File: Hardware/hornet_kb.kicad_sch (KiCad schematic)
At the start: 28 parts, among them J1 Conn_ST_STDC14, J10 USB_C_Receptacle_USB2.0, SW98 SW_Push, U1 nRF52840, Y1 32.768kHz, Y2 32MHz

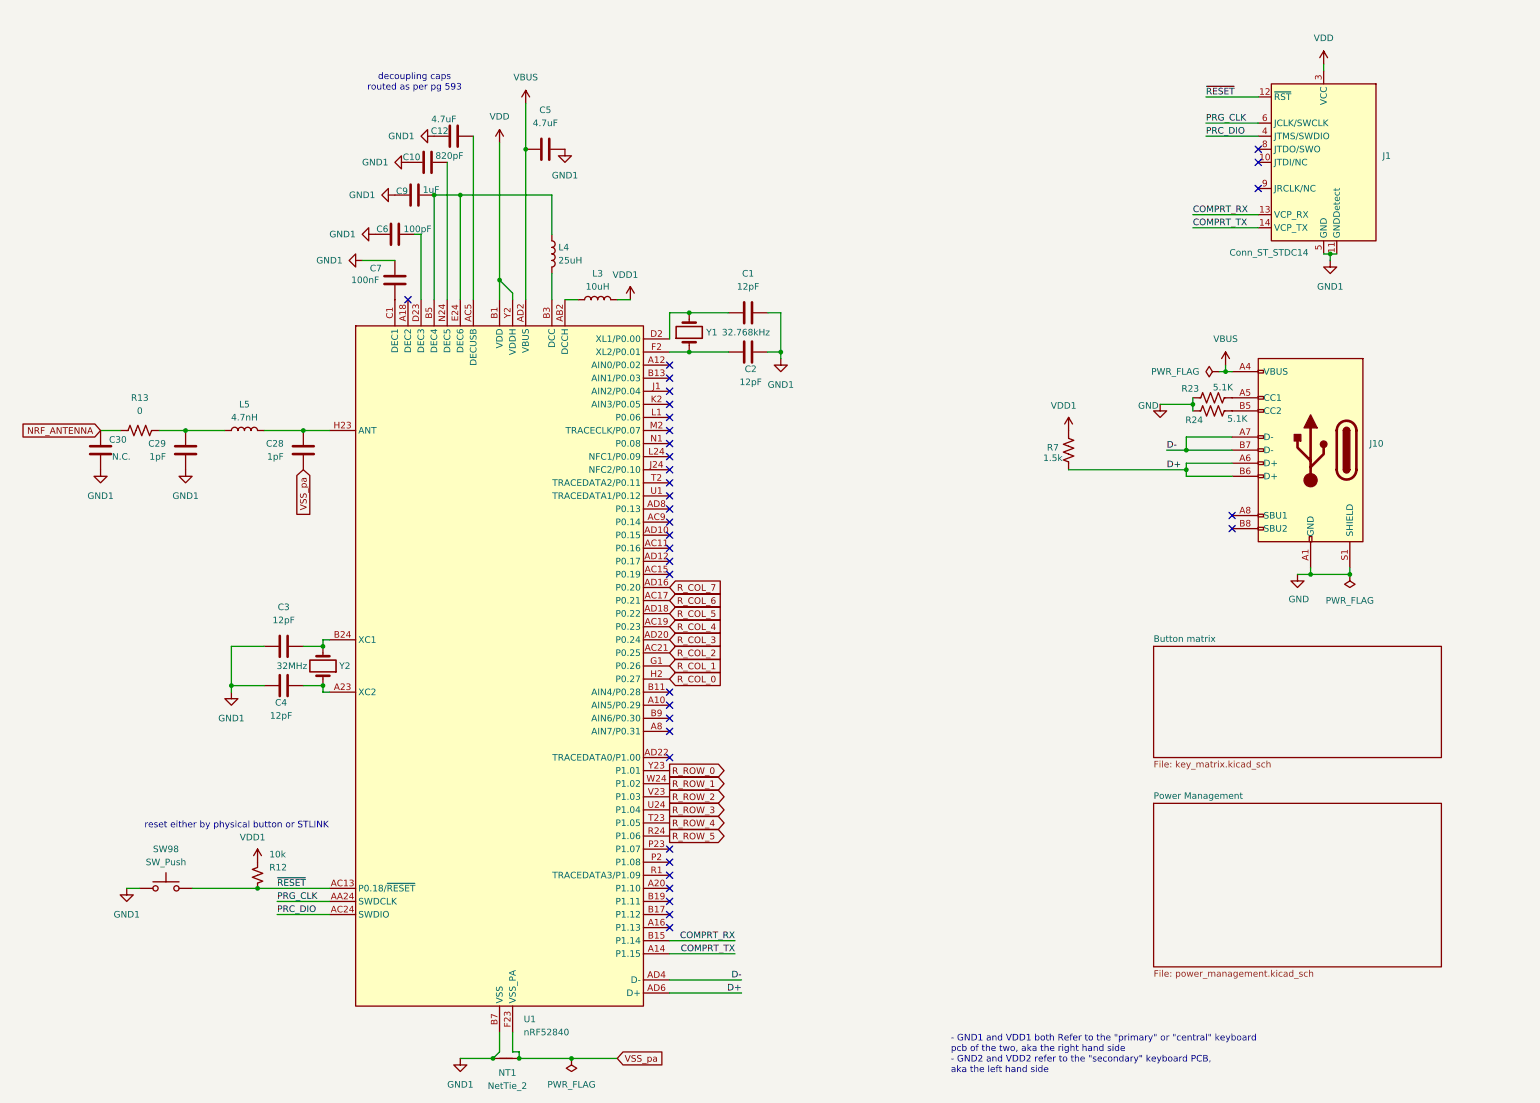
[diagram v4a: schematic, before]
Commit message: Change labels from global to netlist
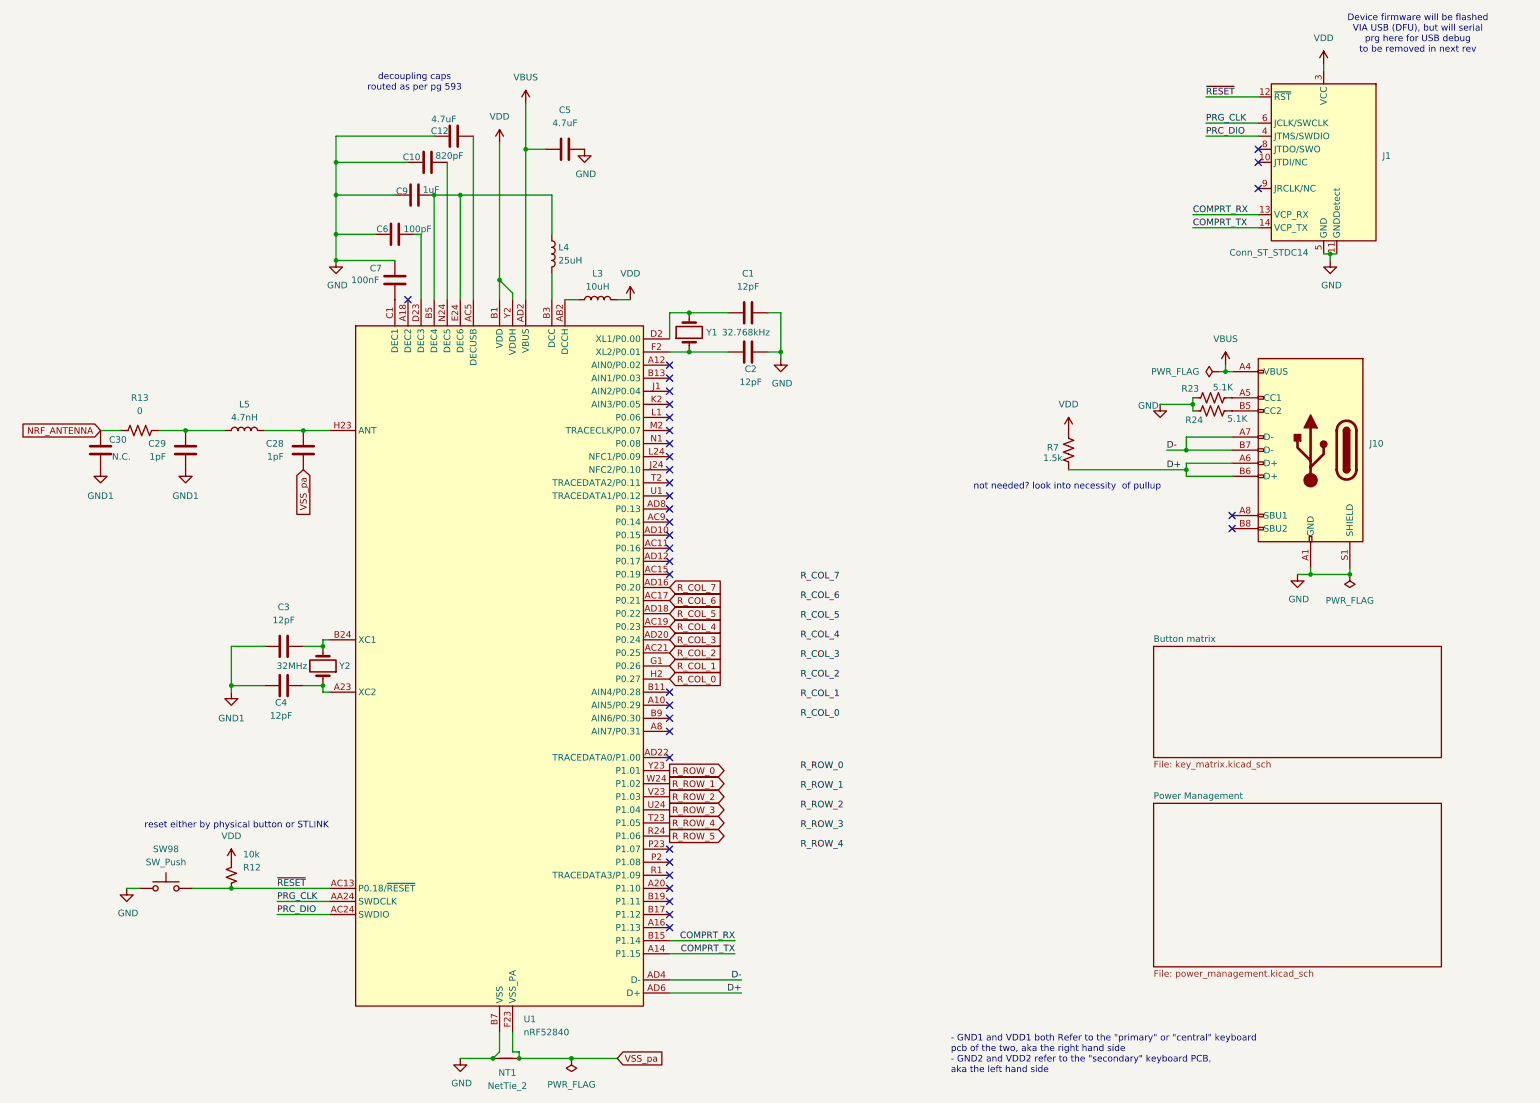
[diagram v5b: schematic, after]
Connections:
- net VDD1 is gone; now on net VDD: L3.1, R12.1, R7.1
- net GND: now also C1.1, C10.1, C12.2, C2.1, C5.1, C6.2, C7.2, C9.2, J1.11 (GNDDetect), J1.5 (GND), J1.7 (GND), NT1.2, SW98.2, U1.B7 (VSS), U1.EP (VSS)
- net GND1: no longer C1.1, C10.1, C12.2, C2.1, C5.1, C6.2, C7.2, C9.2, J1.11 (GNDDetect), J1.5 (GND), J1.7 (GND), NT1.2, SW98.2, U1.B7 (VSS), U1.EP (VSS)
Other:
- note added: "Device firmware will be flashed VIA USB (DFU), but will serial prg here for USB debug to be removed in next rev"
- note added: "not needed? look into necessity of pullup"
- moved on the sheet: C5, R12

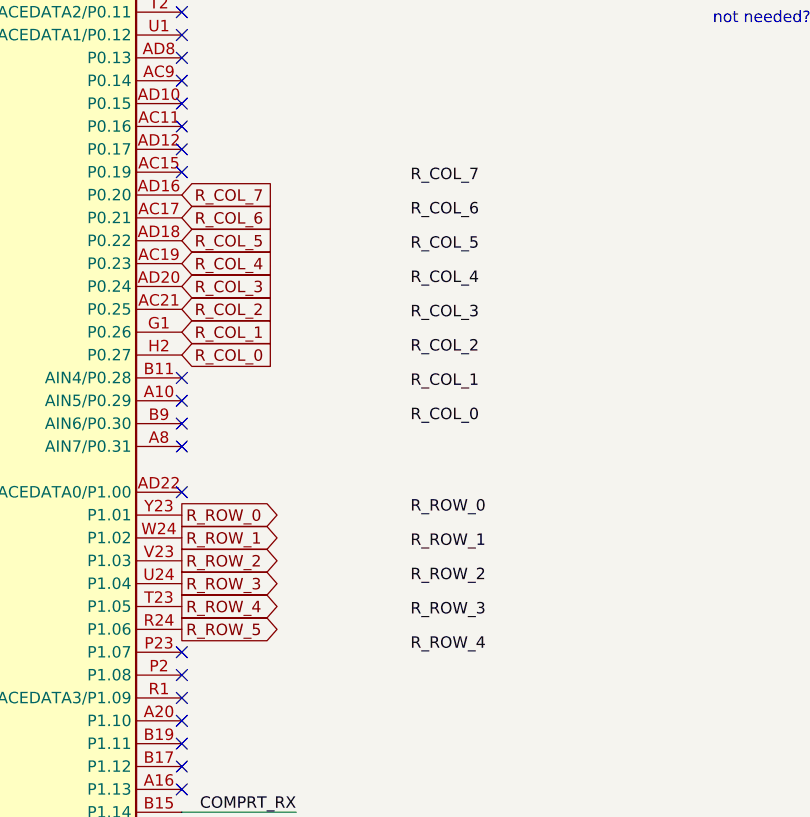
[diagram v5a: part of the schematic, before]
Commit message: Refactor keyboard and power schematics, remove backups
Deleted old hornet_kb schematic backup ZIPs. Updated hornet_kb.kicad_sch: reorganized right-hand row/column labels and wires for physical pin convenience, added annotation, and removed redundant global labels. In power_management.kicad_sch: removed decorative Rx coil circles, updated annotation positions and text, and shifted many schematic elements for improved clarity and layout.
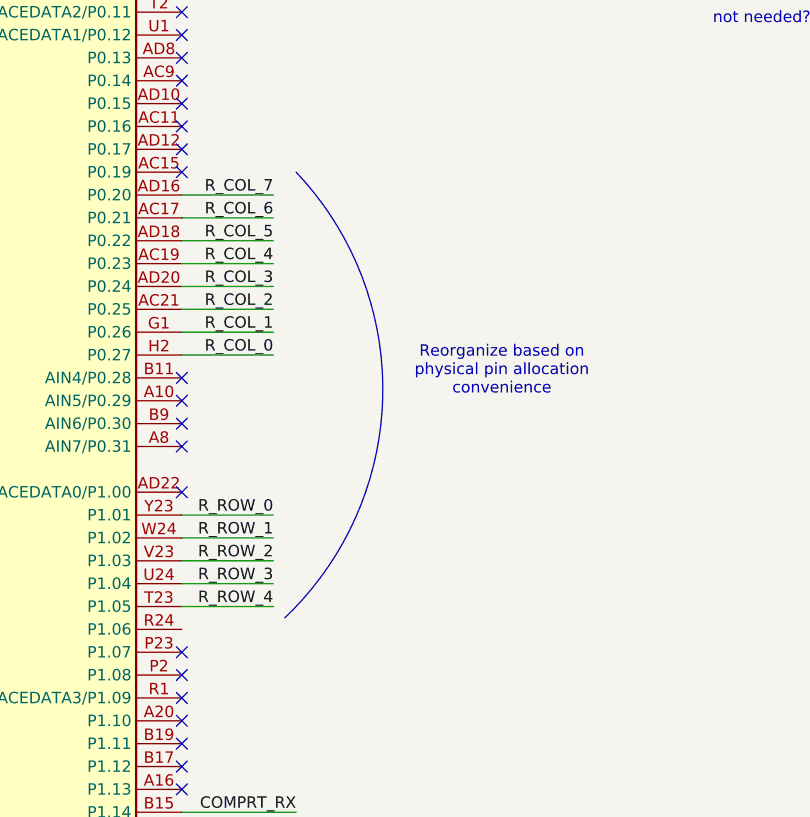
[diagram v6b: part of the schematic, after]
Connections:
- net R_ROW_5: no longer names the net of U1.R24 (P1.06)
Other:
- note added: "Reorganize based on physical pin allocation convenience"

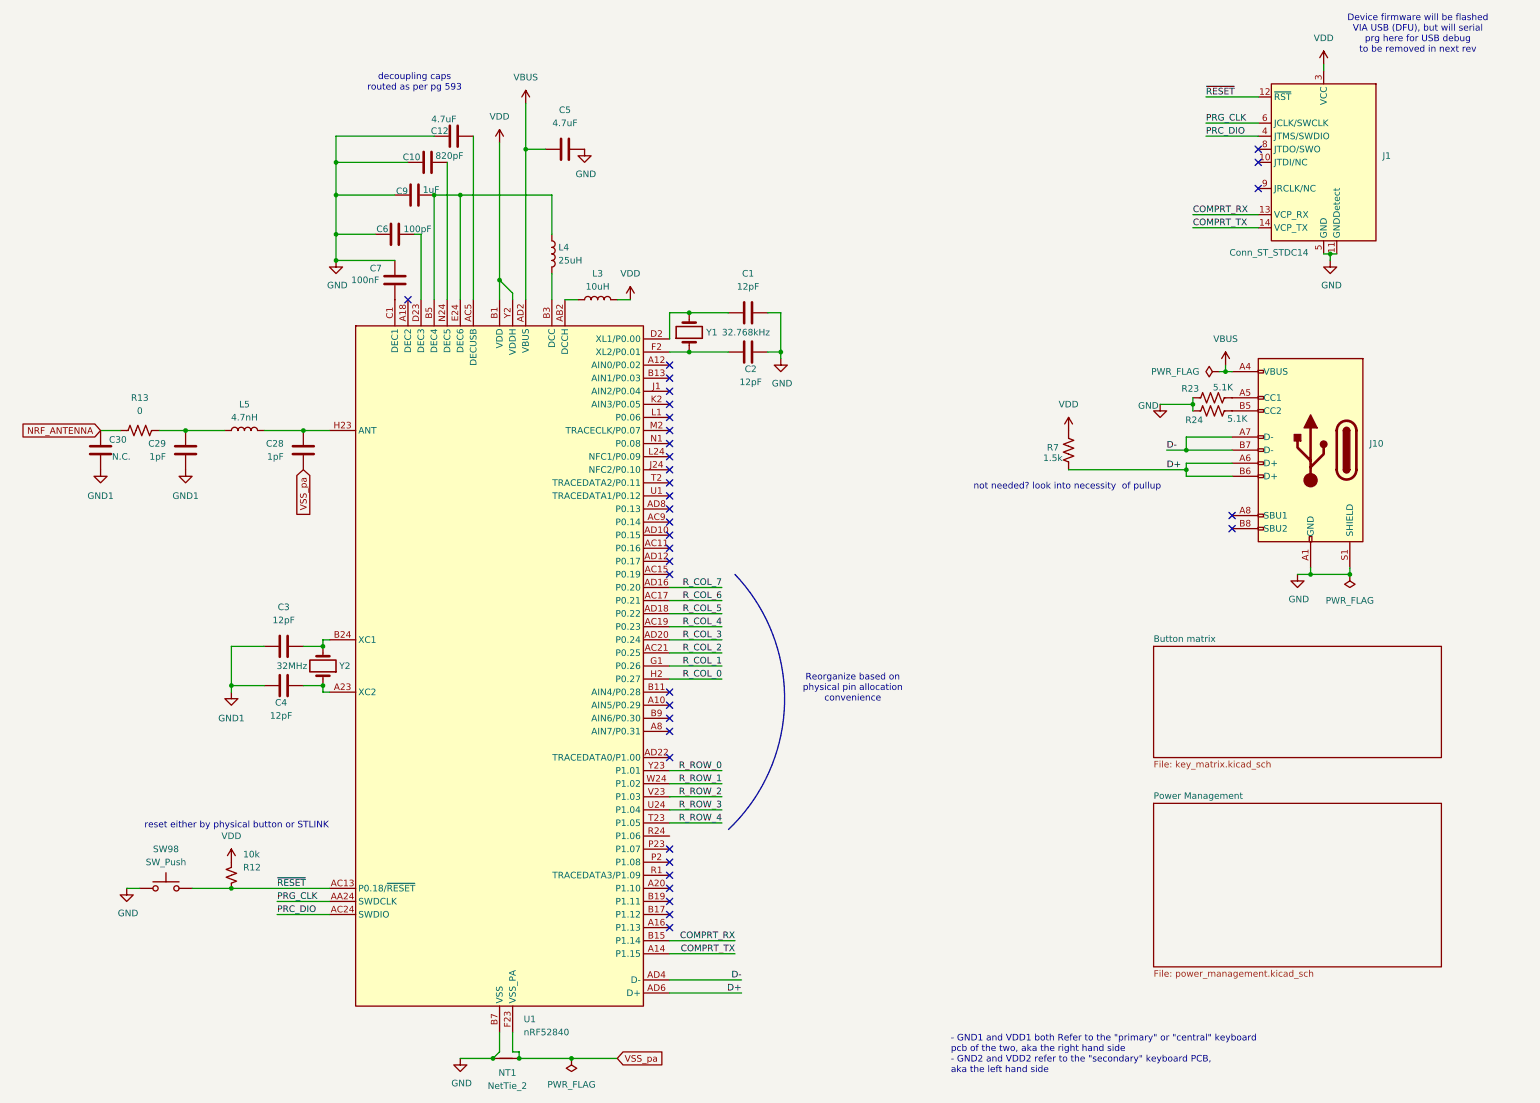
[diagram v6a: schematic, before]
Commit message: Update schematic coordinates and add notes
Adjusted coordinates for wires, junctions, and no_connects in hornet_kb.kicad_sch for improved layout clarity. Added company info and new design notes. Deleted outdated backup ZIP file.
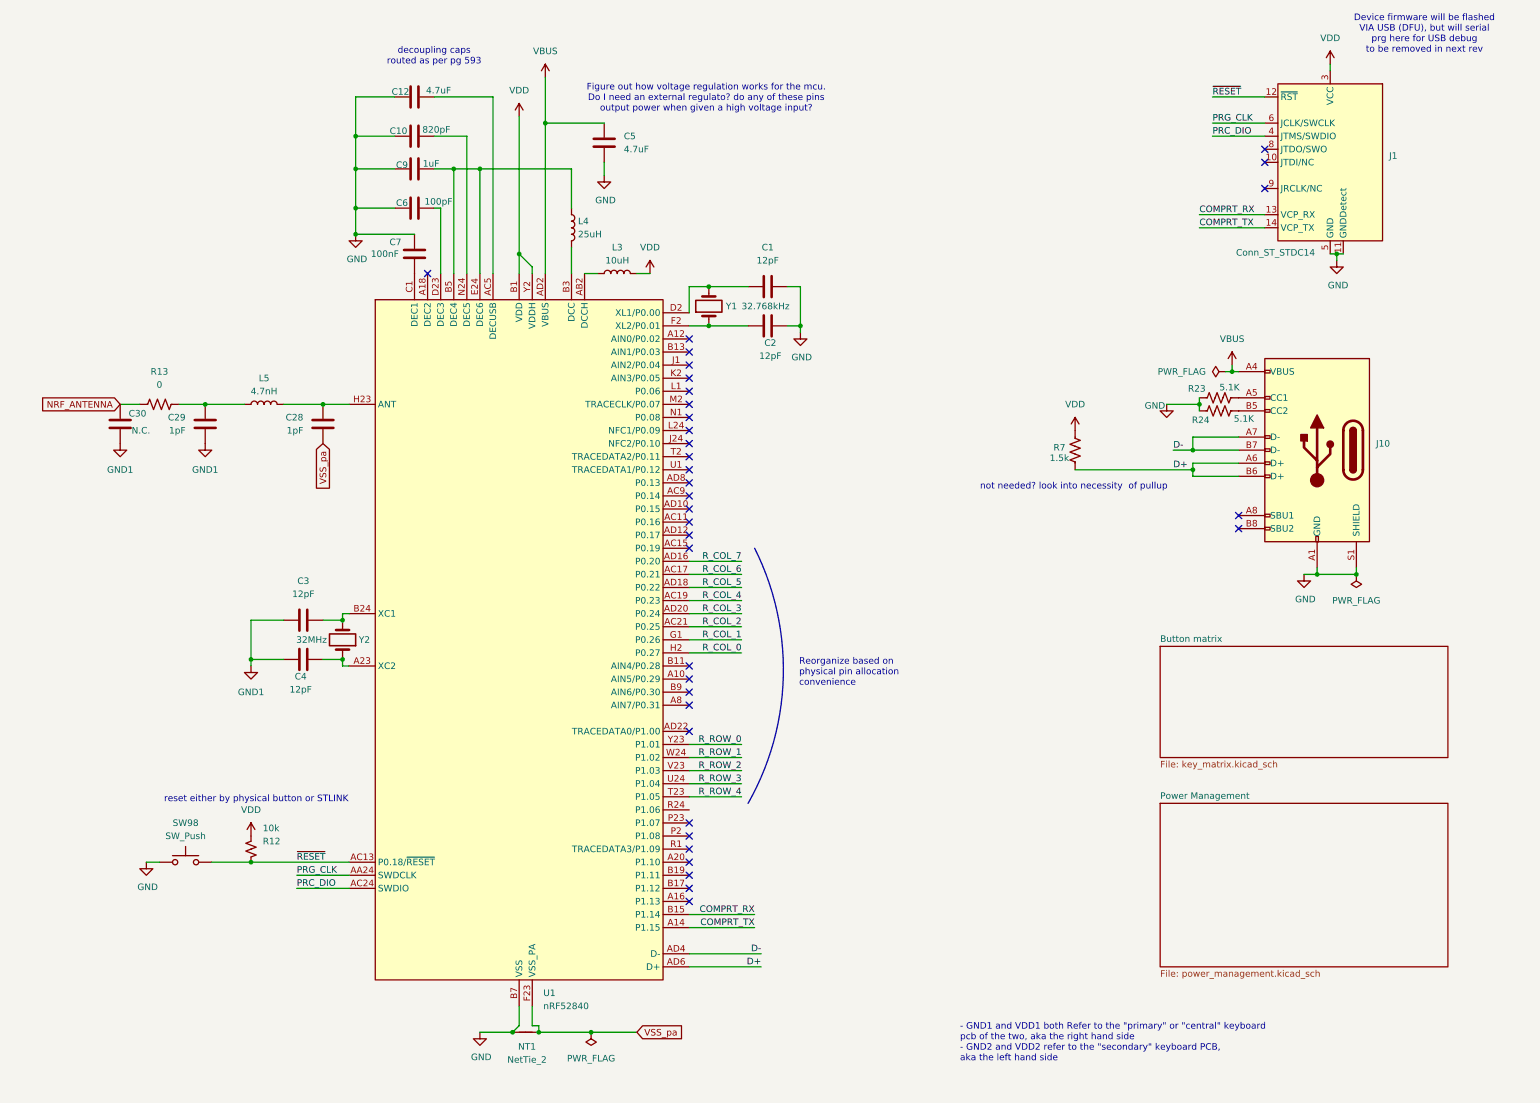
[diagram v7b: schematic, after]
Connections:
- net GND: now also C5.2; no longer C5.1
- net VBUS: now also C5.1; no longer C5.2
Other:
- note added: "Figure out how voltage regulation works for the mcu. Do I need an external regulato? do any of these pins output power when given a high voltage input?"
- company: (none) -> Aryan & Friends :D
- moved on the sheet: C1, C10, C12, C2, C28, C29, C3, C30, C4, C5, C6, C7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
